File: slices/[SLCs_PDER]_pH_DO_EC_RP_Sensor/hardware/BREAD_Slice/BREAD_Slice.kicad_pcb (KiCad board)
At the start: 2 copper layers, 70 x 100 mm, 9 parts, among them J1 Conn_01x10_Female

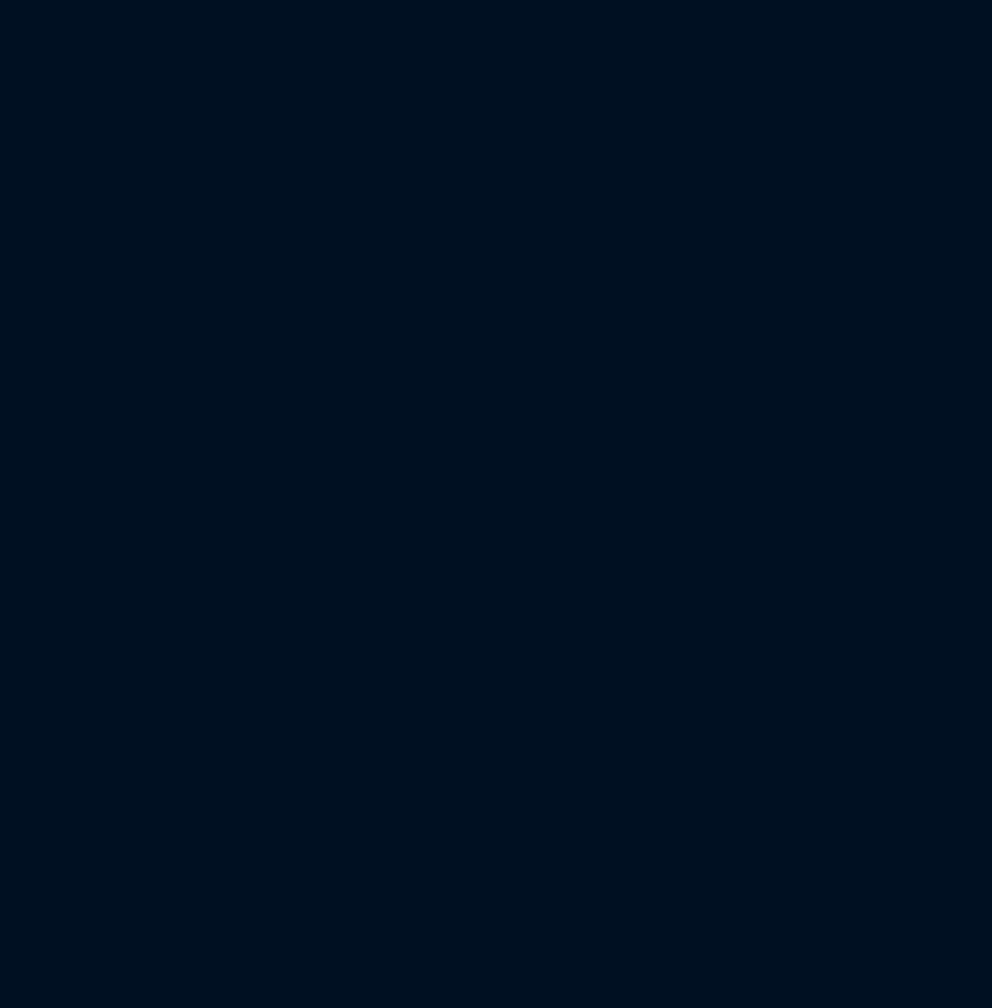
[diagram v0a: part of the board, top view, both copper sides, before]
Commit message: improved phdo and initial ERC pass on PDER
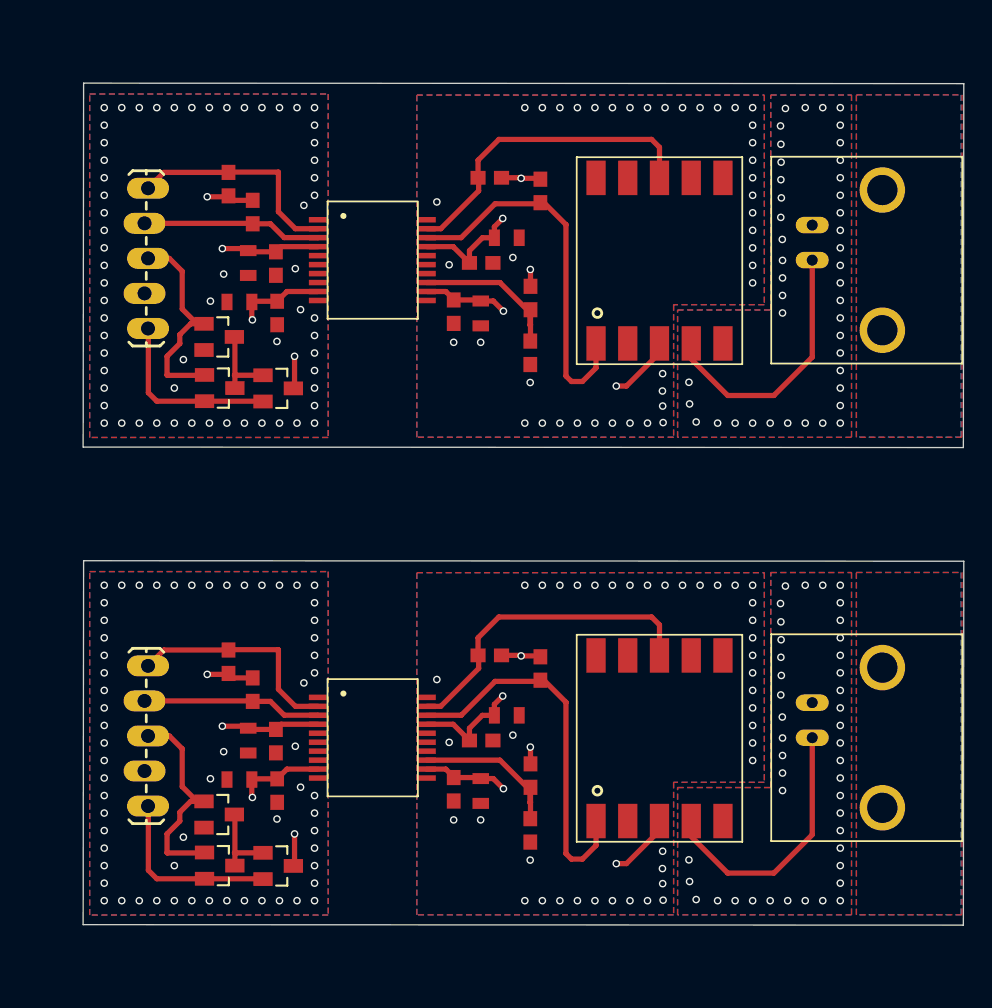
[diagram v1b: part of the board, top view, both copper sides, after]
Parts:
- added C1: 10uF, ADM3260_Breakout:0805, F.Cu at (214.6, 66.9)
- added C1: 10uF, ADM3260_Breakout:0805, F.Cu at (214.6, 101.5)
- added C2: 0.1uF, ADM3260_Breakout:0603, F.Cu at (217.3, 102.3)
- added C2: 0.1uF, ADM3260_Breakout:0603, F.Cu at (217.3, 67.7)
- added C3: 10uF, ADM3260_Breakout:0805, F.Cu at (215.2, 98.7)
- added C3: 10uF, ADM3260_Breakout:0805, F.Cu at (215.2, 64.1)
- added C4: 0.1uF, ADM3260_Breakout:0603, F.Cu at (217.2, 64.1)
- added C4: 0.1uF, ADM3260_Breakout:0603, F.Cu at (217.2, 98.7)
- added C5: 0.1uF, ADM3260_Breakout:0603, F.Cu at (230.1, 102.2)
- added C5: 0.1uF, ADM3260_Breakout:0603, F.Cu at (230.1, 67.6)
- added C6: 10uF, ADM3260_Breakout:0805, F.Cu at (232.1, 67.7)
- added C6: 10uF, ADM3260_Breakout:0805, F.Cu at (232.1, 102.3)
- added C7: 0.1uF, ADM3260_Breakout:0603, F.Cu at (232.1, 64.1)
- added C7: 0.1uF, ADM3260_Breakout:0603, F.Cu at (232.1, 98.7)
- added C8: 10uF, ADM3260_Breakout:0805, F.Cu at (233.9, 62.3)
- added C8: 10uF, ADM3260_Breakout:0805, F.Cu at (233.9, 96.9)
- added J1: , ADM3260_Breakout:1X05_LOCK_LONGPADS, F.Cu at (207.9, 58.7)
- added J1: , ADM3260_Breakout:1X05_LOCK_LONGPADS, F.Cu at (207.9, 93.3)
- added J2: BNCPTH, ADM3260_Breakout:BNC, F.Cu at (256.1, 98.5)
- added J2: BNCPTH, ADM3260_Breakout:BNC, F.Cu at (256.1, 63.9)
- added Q1: PMV32UP, ADM3260_Breakout:SOT23, F.Cu at (213.1, 107.8)
- added Q1: PMV32UP, ADM3260_Breakout:SOT23, F.Cu at (213.1, 73.1)
- added Q2: PMV16XN, ADM3260_Breakout:SOT23, F.Cu at (213.1, 104.0)
- added Q2: PMV16XN, ADM3260_Breakout:SOT23, F.Cu at (213.1, 69.4)
- added Q3: PMV32UP, ADM3260_Breakout:SOT23, F.Cu at (217.4, 107.8)
- added Q3: PMV32UP, ADM3260_Breakout:SOT23, F.Cu at (217.4, 73.2)
- added R1: 4.7k, ADM3260_Breakout:0603, F.Cu at (213.8, 93.0)
- added R1: 4.7k, ADM3260_Breakout:0603, F.Cu at (213.8, 58.4)
- added R2: 4.7k, ADM3260_Breakout:0603, F.Cu at (215.5, 95.0)
- added R2: 4.7k, ADM3260_Breakout:0603, F.Cu at (215.5, 60.4)
- added R3: 4.7k, ADM3260_Breakout:0603, F.Cu at (236.4, 58.9)
- added R3: 4.7k, ADM3260_Breakout:0603, F.Cu at (236.4, 93.5)
- added R4: 4.7k, ADM3260_Breakout:0603, F.Cu at (232.7, 57.9)
- added R4: 4.7k, ADM3260_Breakout:0603, F.Cu at (232.7, 92.5)
- added R5: 16.2k, ADM3260_Breakout:0603, F.Cu at (235.7, 66.6)
- added R5: 16.2k, ADM3260_Breakout:0603, F.Cu at (235.7, 101.2)
- added R6: 10k, ADM3260_Breakout:0603, F.Cu at (235.6, 105.2)
- added R6: 10k, ADM3260_Breakout:0603, F.Cu at (235.6, 70.6)
- added U1: ADM3260, ADM3260_Breakout:ADM3260, F.Cu at (224.2, 98.5)
- added U1: ADM3260, ADM3260_Breakout:ADM3260, F.Cu at (224.2, 63.9)
- added U2: Atlas Scientific OEM pH or ORP, ADM3260_Breakout:PHSENSOR, F.Cu at (245.0, 98.5)
- added U2: Atlas Scientific OEM pH or ORP, ADM3260_Breakout:PHSENSOR, F.Cu at (245.0, 63.9)
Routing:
- net GND-ISO: track 0.00 -> 110.6 mm, vias 0 -> 84
- net SDA1: track 0.00 -> 54.6 mm
- net 3V3-ISO: track 0.00 -> 46.9 mm, vias 0 -> 10
- net SCL1: track 0.00 -> 46.7 mm
- net AVCC: track 0.00 -> 38.8 mm, vias 0 -> 8
- net PRB: track 0.00 -> 38.3 mm
- net SCL2: track 0.00 -> 32.3 mm
- net EN: track 0.00 -> 31.5 mm
- net VCC: track 0.00 -> 26.5 mm
- net SDA2: track 0.00 -> 26.0 mm
- net N$1: track 0.00 -> 23.2 mm
- net N$2: track 0.00 -> 17.2 mm
- net PRBGND: vias 0 -> 86
- net GND: vias 0 -> 124
- added copper zone on B.Cu, net (none)
- added copper zone on F.Cu, net (none)
- added copper zone on In1.Cu, net (none)
- added copper zone on In2.Cu, net (none)
- added copper zone on In2.Cu, net 3V3-ISO
- added copper zone on In1.Cu, net AVCC
- added copper zone on F.Cu, net GND
- added copper zone on In2.Cu, net GND
- added copper zone on B.Cu, net GND-ISO
- added copper zone on F.Cu, net GND-ISO
- added copper zone on In1.Cu, net GND-ISO
- added copper zone on B.Cu, net PRBGND
- added copper zone on F.Cu, net PRBGND
- added copper zone on In1.Cu, net PRBGND
- added copper zone on In2.Cu, net PRBGND
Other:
- board size 70 x 100 mm -> 144.5 x 100 mm
- copper layers 2 -> 4
- rule pad_to_mask_clearance: 0.05 -> 0

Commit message: atlas oem slice footprints all done and at routing stage
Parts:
- removed the C1 at (156.4, 100.0)
- added ?: , RPI_Hat:RPi_Hat_Mounting_Hole, F.Cu at (220.5, 99.6)
- added ?: , RPI_Hat:RPi_Hat_Mounting_Hole, F.Cu at (269.5, 99.6)
- added ?: , RPI_Hat:RPi_Hat_Mounting_Hole, F.Cu at (269.5, 157.6)
- added ?: , RPI_Hat:RPi_Hat_Mounting_Hole, F.Cu at (220.5, 157.6)
- added C1: 22uF, Capacitor_SMD:C_1206_3216Metric, F.Cu at (150.7, 72.5)
- added C1: 22uF, Capacitor_SMD:C_1206_3216Metric, F.Cu at (42.2, 22.8)
- added C2: 10UF-0805-10V-10%, Capacitor_SMD:C_0805_2012Metric, F.Cu at (78.5, 49.9)
- added C21: 22uF, Capacitor_SMD:C_1206_3216Metric, F.Cu at (151.8, 87.7)
- added C22: 0.1UF-0603-25V-(+80/-20%), Capacitor_SMD:C_0201_0603Metric, F.Cu at (82.0, 51.0)
- added C23: 0.1UF-0603-25V-(+80/-20%), Capacitor_SMD:C_0201_0603Metric, F.Cu at (82.0, 52.8)
- added C24: 0.1UF-0603-25V-(+80/-20%), Capacitor_SMD:C_0201_0603Metric, F.Cu at (82.0, 54.5)
- added C25: 10UF-0805-10V-10%, Capacitor_SMD:C_0805_2012Metric, F.Cu at (78.5, 55.9)
- added C26: 10UF-0805-10V-10%, Capacitor_SMD:C_0805_2012Metric, F.Cu at (78.5, 58.9)
- added C27: 10UF-0805-10V-10%, Capacitor_SMD:C_0805_2012Metric, F.Cu at (78.5, 93.0)
- added C28: 10UF-0805-10V-10%, Capacitor_SMD:C_0805_2012Metric, F.Cu at (78.5, 96.1)
- added C29: 0.1UF-0603-25V-(+80/-20%), Capacitor_SMD:C_0201_0603Metric, F.Cu at (82.0, 92.4)
- added C3: 10UF-0805-10V-10%, Capacitor_SMD:C_0805_2012Metric, F.Cu at (78.5, 52.9)
- added C30: 0.1UF-0603-25V-(+80/-20%), Capacitor_SMD:C_0201_0603Metric, F.Cu at (82.0, 94.2)
- added C31: 0.1UF-0603-25V-(+80/-20%), Capacitor_SMD:C_0201_0603Metric, F.Cu at (82.0, 95.9)
- added C32: 0.1UF-0603-25V-(+80/-20%), Capacitor_SMD:C_0201_0603Metric, F.Cu at (82.0, 97.7)
- added C33: 10UF-0805-10V-10%, Capacitor_SMD:C_0805_2012Metric, F.Cu at (78.5, 99.1)
- added C34: 10UF-0805-10V-10%, Capacitor_SMD:C_0805_2012Metric, F.Cu at (78.5, 102.1)
- added C4: 0.1UF-0603-25V-(+80/-20%), Capacitor_SMD:C_0201_0603Metric, F.Cu at (82.0, 49.2)
- added C5: 100nF, Capacitor_SMD:C_1206_3216Metric, F.Cu at (42.2, 26.1)
- added C6: 22uF, Capacitor_SMD:C_1206_3216Metric, F.Cu at (42.2, 29.4)
- added C7: 22uF, Capacitor_SMD:C_1206_3216Metric, F.Cu at (42.2, 32.8)
- added D1: WS2812B_5050, SparkFun-LED:WS2812-5050-4PIN, F.Cu at (39.0, 65.1)
- added H1: MountingHole, MountingHole:MountingHole_5mm, F.Cu at (20.3, 26.9)
- added H2: MountingHole, MountingHole:MountingHole_5mm, F.Cu at (20.3, 38.4)
- added H3: MountingHole, MountingHole:MountingHole_5mm, F.Cu at (20.3, 50.0)
- added H4: MountingHole, MountingHole:MountingHole_5mm, F.Cu at (20.3, 61.5)
- added HS1: Heatsink_Pad, KML-Custom:Thermal Pad, F.Cu at (45.9, 41.0)
- added J1: RPi_GPIO, RPI_Hat:Samtec_HLE-120-02-XXX-DV-BE-XX-XX, F.Cu at (220.6, 128.6)
- added J1: I2C_01x04, Connector_JST:JST_SH_SM04B-SRSS-TB_1x04-1MP_P1.00mm_Horizontal, F.Cu at (30.5, 65.6)
- added J11: CONN_05LOCK_LONGPADS, Connector_JST:JST_EH_B5B-EH-A_1x05_P2.50mm_Vertical, F.Cu at (74.7, 36.0)
- added J2: Conn_01x10_Female, Connector_PinSocket_2.54mm:PinSocket_1x10_P2.54mm_Horizontal, F.Cu at (37.1, 23.4)
- added J2: RPi_GPIO, RPI_Hat:Pin_Header_Straight_2x20, F.Cu at (220.6, 128.6)
- added J22: BNCPTH, Connector_Coaxial:BNC_Amphenol_B6252HB-NPP3G-50_Horizontal, F.Cu at (62.8, 55.4)
- added J3: CONN_05LOCK_LONGPADS, Connector_JST:JST_EH_B5B-EH-A_1x05_P2.50mm_Vertical, F.Cu at (74.7, 79.2)
- added J4: BNCPTH, Connector_Coaxial:BNC_Amphenol_B6252HB-NPP3G-50_Horizontal, F.Cu at (62.8, 98.6)
- added L1: 4.7uH, Inductor_SMD:L_1210_3225Metric, F.Cu at (46.0, 63.9)
- added Q1: BSS84, Package_TO_SOT_SMD:SOT-23-3, F.Cu at (73.8, 50.8)
- added Q2: BSH105, Package_TO_SOT_SMD:SOT-23-3, F.Cu at (73.8, 55.4)
- added Q3: BSS84, Package_TO_SOT_SMD:SOT-23-3, F.Cu at (73.8, 60.0)
- added Q4: BSH105, Package_TO_SOT_SMD:SOT-23-3, F.Cu at (73.8, 93.9)
- added Q5: BSS84, Package_TO_SOT_SMD:SOT-23-3, F.Cu at (73.8, 98.6)
- added Q6: BSS84, Package_TO_SOT_SMD:SOT-23-3, F.Cu at (73.8, 103.2)
- added R13: 4.7KOHM-0603-1/10W-1%, Resistor_SMD:R_0201_0603Metric, F.Cu at (82.0, 56.2)
- added R14: 4.7KOHM-0603-1/10W-1%, Resistor_SMD:R_0201_0603Metric, F.Cu at (84.5, 49.2)
- added R15: 4.7KOHM-0603-1/10W-1%, Resistor_SMD:R_0201_0603Metric, F.Cu at (84.5, 51.0)
- added R16: 4.7KOHM-0603-1/10W-1%, Resistor_SMD:R_0201_0603Metric, F.Cu at (84.5, 52.8)
- added R17: 16.2KOHM-0603-1/10W-1%, Resistor_SMD:R_0201_0603Metric, F.Cu at (84.5, 54.5)
- added R18: 10KOHM-0603-1/10W-1%, Resistor_SMD:R_0201_0603Metric, F.Cu at (84.5, 56.2)
- added R19: 4.7KOHM-0603-1/10W-1%, Resistor_SMD:R_0201_0603Metric, F.Cu at (82.0, 99.4)
- added R20: 4.7KOHM-0603-1/10W-1%, Resistor_SMD:R_0201_0603Metric, F.Cu at (84.5, 92.4)
- added R21: 4.7KOHM-0603-1/10W-1%, Resistor_SMD:R_0201_0603Metric, F.Cu at (84.5, 94.2)
- added R22: 4.7KOHM-0603-1/10W-1%, Resistor_SMD:R_0201_0603Metric, F.Cu at (84.5, 95.9)
- added R23: 16.2KOHM-0603-1/10W-1%, Resistor_SMD:R_0201_0603Metric, F.Cu at (84.5, 97.7)
- added R24: 10KOHM-0603-1/10W-1%, Resistor_SMD:R_0201_0603Metric, F.Cu at (84.5, 99.4)
- added SW1: SW_SPDT, SparkFun-Switch:Slide_SPDT_PTH_11.6x4.0mm, F.Cu at (29.1, 55.1)
- added SW2: SW_SPDT, SparkFun-Switch:Slide_SPDT_PTH_11.6x4.0mm, F.Cu at (35.1, 55.1)
- added SW3: SW_SPDT, SparkFun-Switch:Slide_SPDT_PTH_11.6x4.0mm, F.Cu at (41.2, 55.1)
- added SW4: SW_SPDT, SparkFun-Switch:Slide_SPDT_PTH_11.6x4.0mm, F.Cu at (47.2, 55.1)
- added U1: ADM3260ARSZ, ADM3260ARSZ:RS_20_ADI, F.Cu at (76.6, 43.8)
- added U2: ~, Package_TO_SOT_SMD:TSOT-23-6, F.Cu at (47.6, 23.5)
- added U22: Atlas Scientific OEM, Atlas-Scientific:Atlas_OEM, F.Cu at (72.8, 32.6)
- added U3: Atlas Scientific OEM, Atlas-Scientific:Atlas_OEM, F.Cu at (72.8, 75.8)
- added U4: ADM3260ARSZ, ADM3260ARSZ:RS_20_ADI, F.Cu at (76.6, 87.0)
- moved J2 153.5 mm to (123.6, 176.0), turned to 180 degrees
- moved J2 153.4 mm to (151.6, 176.2), turned to 180 degrees
- moved U2 138.4 mm to (123.6, 165.0), turned to 0 degrees
- moved U2 137.7 mm to (151.6, 165.1), turned to 0 degrees
- moved R6 129.0 mm to (116.9, 155.6), turned to 0 degrees
- moved R5 127.0 mm to (120.9, 155.6), turned to 0 degrees
- moved R3 126.1 mm to (156.7, 156.5), turned to 0 degrees
- moved R3 124.7 mm to (128.7, 156.3), turned to 0 degrees
- moved R6 124.4 mm to (144.9, 155.8), turned to 0 degrees
- moved R5 124.4 mm to (148.9, 155.8), turned to 0 degrees
- moved C6 122.8 mm to (119.8, 152.0), turned to 180 degrees
- moved C8 122.7 mm to (125.3, 153.9), turned to -90 degrees
- moved C8 122.2 mm to (153.3, 154.1), turned to -90 degrees
- moved C7 121.1 mm to (123.4, 152.0), turned to -90 degrees
- moved R4 121.0 mm to (157.6, 152.8), turned to -90 degrees
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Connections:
- A1 pad 10: /BR2 -> /EN2
- A1 pad 11: /THRM2 -> /RX1
- A1 pad 12: /DIR1 -> /TX1
- A1 pad 13: /MC1 -> /RX2
- A1 pad 14: /BR1 -> /TX2
- A1 pad 15: /THRM1 -> unconnected-(A1-D12-Pad15)
- A1 pad 19: /A1 -> unconnected-(A1-A0-Pad19)
- A1 pad 20: /B1 -> unconnected-(A1-A1-Pad20)
- A1 pad 21: /A2 -> unconnected-(A1-A2-Pad21)
- A1 pad 22: /B2 -> unconnected-(A1-A3-Pad22)
- A1 pad 25: /CSEN1 -> unconnected-(A1-A6-Pad25)
- A1 pad 26: /CSEN2 -> unconnected-(A1-A7-Pad26)
- A1 pad 30: +12V -> unconnected-(A1-VIN-Pad30)
- A1 pad 8: /DIR2 -> /LED
- A1 pad 9: /MC2 -> /EN1
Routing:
- net +12V: track 45.5 -> 41.9 mm
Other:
- board size 144.5 x 100 mm -> 163 x 174.9 mm
